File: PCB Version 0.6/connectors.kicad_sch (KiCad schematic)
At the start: 35 parts, among them J5 Conn_01x08_MountingPin, J6 Conn_01x06_MountingPin, J7 Conn_01x06_MountingPin

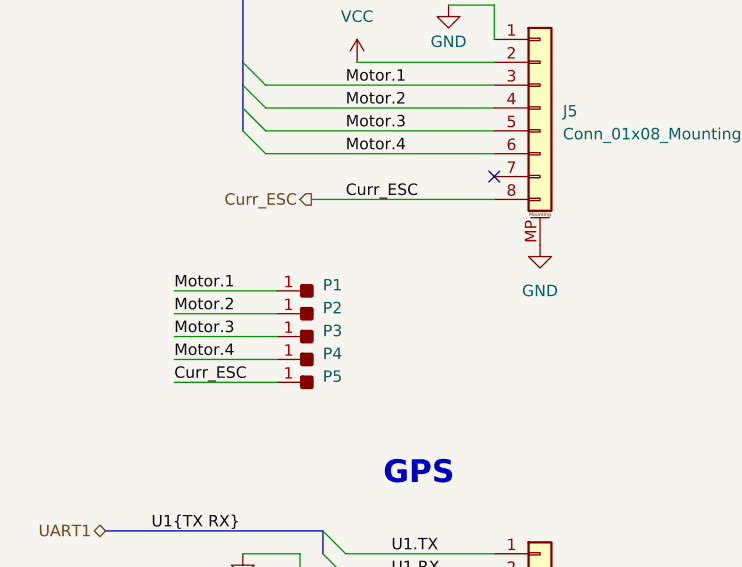
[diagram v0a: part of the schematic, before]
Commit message: remove current sensor ADC, swap opamp, add dcdc switch
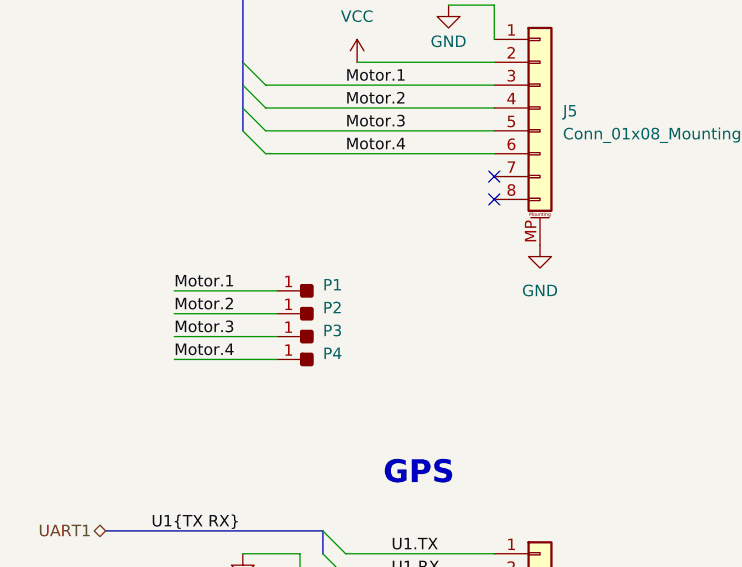
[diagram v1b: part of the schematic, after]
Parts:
- removed P5: ~, Kolibri custom:Solder_Pad_rounded, symbol Kolibri custom:Solder_Pad_rounded
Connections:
- net Curr_ESC: no longer names the net of J5.8 (Pin_8)
- no-connect marks 2 -> 3
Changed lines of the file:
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@@
 	)
 	(no_connect
+		(at 71.12 55.88)
+	)
+	(no_connect
 		(at 71.12 53.34)
 	)
@@
 	(wire
 		(pts
-			(xy 50.8 55.88) (xy 71.12 55.88)
-		)
-		(stroke
-			(width 0)
-			(type default)
-		)
-	)
-	(wire
-		(pts
 			(xy 66.04 162.56) (xy 66.04 167.64)
 		)
@@
 		)
 	)
-	(wire
-		(pts
-			(xy 35.56 76.2) (xy 46.99 76.2)
-		)
-		(stroke
-			(width 0)
-			(type default)
-		)
-	)
 	(bus
 		(pts
@@
 		)
 	)
-	(label "Curr_ESC"
-		(at 54.61 55.88 0)
-		(effects
-			(font
-				(size 1.27 1.27)
-			)
-			(justify left bottom)
-		)
-	)
 	(label "Motor.1"
 		(at 54.61 43.18 0)
@@
 		)
 	)
-	(label "Curr_ESC"
-		(at 35.56 76.2 0)
-		(effects
-			(font
-				(size 1.27 1.27)
-			)
-			(justify left bottom)
-		)
-	)
 	(label "U2.RX"
 		(at 58.42 160.02 0)
@@
 		)
 	)
-	(hierarchical_label "Curr_ESC"
-		(shape output)
-		(at 50.8 55.88 180)
-		(effects
-			(font
-				(size 1.27 1.27)
-			)
-			(justify right)
-		)
-	)
 	(hierarchical_label "Motors"
 		(shape bidirectional)
@@
 					(unit 1)
 				)
-			)
-		)
-	)
-	(symbol
-		(lib_id "Kolibri custom:Solder_Pad_rounded")
-		(at 49.53 76.2 0)
-		(unit 1)
-		(exclude_from_sim no)
-		(in_bom yes)
-		(on_board yes)
-		(dnp no)
-		(fields_autoplaced yes)
-		(property "Reference" "P5"
-			(at 52.07 75.5649 0)
-			(effects
-				(font
-					(size 1.27 1.27)
-				)
-				(justify left)
-			)
-		)
-		(property "Value" "~"
-			(at 52.07 77.47 0)
-			(effects
-				(font
-					(size 1.27 1.27)
-				)
-				(justify left)
-			)
-		)
-		(property "Footprint" "Kolibri custom:Solder_Pad_rounded"
-			(at 49.53 76.2 0)
-			(effects
-				(font
-					(size 1.27 1.27)
-				)
-				(hide yes)
-			)
-		)
-		(property "Datasheet" ""
-			(at 49.53 76.2 0)
-			(effects
-				(font
-					(size 1.27 1.27)
-				)
-				(hide yes)
-			)
-		)
-		(property "Description" ""
-			(at 49.53 76.2 0)
-			(effects
-				(font
-					(size 1.27 1.27)
-				)
-				(hide yes)
-			)
-		)
-		(pin "1"
-		)
-		(instances
-			(project "Kolibri v0.5"
-				(path "/1651f454-30c0-48ea-9fcf-6c96a661786a/c061bb86-7a8e-4300-a3f9-744e498f6d03"
-					(reference "P5")
-					(unit 1)
-				)

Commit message: wip layout
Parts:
- removed P18, P19: ~, Kolibri custom:Solder_Pad_rounded_dual, symbol Kolibri custom:Solder_Pad_rounded_dual
- added P18, P5: ~, Kolibri custom:Solder_Pad_rounded, symbol Kolibri custom:Solder_Pad_rounded
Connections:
- net Video.In: now also P5.1
- net Video.Out: now also P18.1

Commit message: wip layout
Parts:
- removed P20, P21, P22: ~, Kolibri custom:Solder_Pad_rounded_dual, symbol Kolibri custom:Solder_Pad_rounded_dual
- removed P25: ~, Kolibri custom:Solder_Pad_rect_dual, symbol Kolibri custom:Solder_Pad_rect_dual
- removed P29, P30: ~, Kolibri custom:Solder_Pad_octa_dual, symbol Kolibri custom:Solder_Pad_octa_dual
- added P19, P20, P21: ~, Kolibri custom:Solder_Pad_rounded, symbol Kolibri custom:Solder_Pad_rounded
- added P22: ~, Kolibri custom:Solder_Pad_rect, symbol Kolibri custom:Solder_Pad_rect
- added P25, P29: ~, Kolibri custom:Solder_Pad_octa, symbol Kolibri custom:Solder_Pad_octa
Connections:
- net +5V: now also P25.1, P29.1
- net GND: now also P22.1
- net LED: now also P21.1
- net Spk.+: now also P19.1
- net Spk.-: now also P20.1

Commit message: layout first draft done
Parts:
- removed P23, P24: ~, Kolibri custom:Solder_Pad_rect_dual, symbol Kolibri custom:Solder_Pad_rect_dual
- removed P28, P33, P34: ~, Kolibri custom:Solder_Pad_octa_dual, symbol Kolibri custom:Solder_Pad_octa_dual
- added P23, P24, P40, P42, P43: ~, Kolibri custom:Solder_Pad_rect, symbol Kolibri custom:Solder_Pad_rect
- added P28, P30, P33, P34, P39, P41: ~, Kolibri custom:Solder_Pad_octa, symbol Kolibri custom:Solder_Pad_octa
- added P37, P38: ~, Kolibri custom:Solder_Pad_rounded, symbol Kolibri custom:Solder_Pad_rounded
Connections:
- net +10V: now also P28.1, P34.1
- net +3V3: now also P30.1, P41.1
- net +5V: now also P39.1
- net GND: now also P23.1, P24.1, P40.1, P42.1, P43.1
- net VCC: now also P33.1
- new net PWM.1: P37.1
- new net PWM.2: P38.1

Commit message: wip routing
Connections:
- net I2C0.SCL: now also J6.5 (Pin_5); no longer J6.6 (Pin_6)
- net I2C0.SDA: now also J6.6 (Pin_6); no longer J6.5 (Pin_5)
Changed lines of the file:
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@@
 		)
 	)
-	(label "I2C0.SDA"
+	(label "I2C0.SCL"
 		(at 58.42 105.41 0)
 		(effects
@@
 		)
 	)
-	(label "I2C0.SCL"
+	(label "I2C0.SDA"
 		(at 58.42 107.95 0)
 		(effects

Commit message: wip
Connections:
- net PWM.1: now also P38.1; no longer P37.1
- net PWM.2: now also P37.1; no longer P38.1
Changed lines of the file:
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@@
 		)
 	)
-	(label "PWM.1"
+	(label "PWM.2"
 		(at 148.59 27.94 0)
 		(effects
@@
 		)
 	)
-	(label "PWM.2"
+	(label "PWM.1"
 		(at 148.59 30.48 0)
 		(effects
